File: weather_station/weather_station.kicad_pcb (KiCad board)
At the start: 2 copper layers, 72.5 x 42.5 mm, 76 parts, among them J1 USB_C_Receptacle_USB2.0_16P, Q1 PMOS, Q2 S8050, Q3 S8050, SW1 SW_Push, SW2 SW_Push, SW3 SW_Push, U2 TLV62569, U3 TP4056-42-ESOP8, U5 Ai-Thinker-Ra-02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

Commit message: Adjusting components
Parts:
- added H2: MountingHole, weather_station_lib:mounting_hole_2, F.Cu at (81.8, 92.0)
- added H3: MountingHole, weather_station_lib:mounting_hole_2, F.Cu at (143.8, 92.0)
- added H4: MountingHole, weather_station_lib:mounting_hole_2, F.Cu at (143.8, 127.0)
- H1: footprint weather_station_lib:mounting_hole_1.5 -> weather_station_lib:mounting_hole_2
- J1: footprint Connector_USB:USB_C_Receptacle_GCT_USB4105-xx-A_16P_TopMnt_Horizontal -> weather_station_lib:USB_C_Receptacle_GCT_USB4105-xx-A_16P_TopMnt_Horizontal_fix_clearance
- U1: footprint weather_station_lib:ESP32-WROOM-32 or ESP32S -> weather_station_lib:ESP32-WROOM-32 or ESP32S_no_paste
- U5: footprint RF_Module:Ai-Thinker-Ra-01-LoRa -> weather_station_lib:Ai-Thinker-Ra-01-LoRa_no_paste
- moved R15 181.1 mm to (87.6, 98.0)
- moved R13 179.8 mm to (87.6, 96.0), turned to 180 degrees
- moved C13 142.8 mm to (120.0, 95.0), turned to 180 degrees
- moved C14 141.9 mm to (119.8, 92.4), turned to 180 degrees
- moved TP1 140.2 mm to (86.4, 127.6)
- moved C17 137.7 mm to (110.6, 96.0), turned to 180 degrees
- moved C18 133.2 mm to (114.8, 96.8)
- moved R8 124.5 mm to (99.6, 94.8)
- moved U4 123.2 mm to (130.3, 96.5), turned to 90 degrees
- moved R18 123.2 mm to (90.8, 108.0)
- moved R11 122.9 mm to (124.3, 126.0)
- moved C8 122.9 mm to (122.3, 125.8)
- moved R2 122.8 mm to (103.4, 92.8), turned to 180 degrees
- moved Q3 122.5 mm to (95.8, 115.2), turned to 90 degrees
- moved R26 121.8 mm to (99.2, 112.2), turned to 0 degrees
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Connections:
- U6 pad 1: GND -> /SDA1
- U6 pad 2: +Vin -> /SCL1
- U6 pad 3: /SCL1 -> +Vin
- U6 pad 4: /SDA1 -> GND
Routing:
- net +Vin: track 0.00 -> 106.6 mm, vias 0 -> 3
- net /GPIO0: track 0.00 -> 65.9 mm, vias 0 -> 2
- net /TXD0: track 0.00 -> 56.0 mm, vias 0 -> 3
- net /EN: track 0.00 -> 55.4 mm, vias 0 -> 3
- net /VBAT_S: track 0.00 -> 53.6 mm, vias 0 -> 2
- net /RXD0: track 0.00 -> 52.9 mm, vias 0 -> 2
- net +Vbat: track 0.00 -> 43.9 mm, vias 0 -> 2
- net /SDA0: track 0.00 -> 43.0 mm, vias 0 -> 1
- net /SCL0: track 0.00 -> 40.7 mm, vias 0 -> 1
- net /SDA1: track 0.00 -> 37.7 mm, vias 0 -> 1
- net +Vch: track 0.00 -> 36.0 mm, vias 0 -> 3
- net VDDcp: track 0.00 -> 35.4 mm, vias 0 -> 3
- net /SCL1: track 0.00 -> 33.7 mm, vias 0 -> 1
- net /TFT_RST: track 0.00 -> 30.4 mm, vias 0 -> 1
- net /SPI_CLK: track 0.00 -> 28.6 mm
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- added copper zone on F.Cu, net +Vin
- added copper zone on B.Cu, net GND
- added copper zone on F.Cu, net GND
- added copper zone on F.Cu, net Net-(U2-SW)
- added copper zone on F.Cu, net Vusb
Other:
- board size 72.5 x 42.5 mm -> 67 x 40 mm
- board text added: "+"
- board text added: "-"
- board text added: "CHR"
- board text added: "EKM"
- board text added: "EN"
- board text added: "RX"
- board text added: "Rev0.1"
- board text added: "TX"

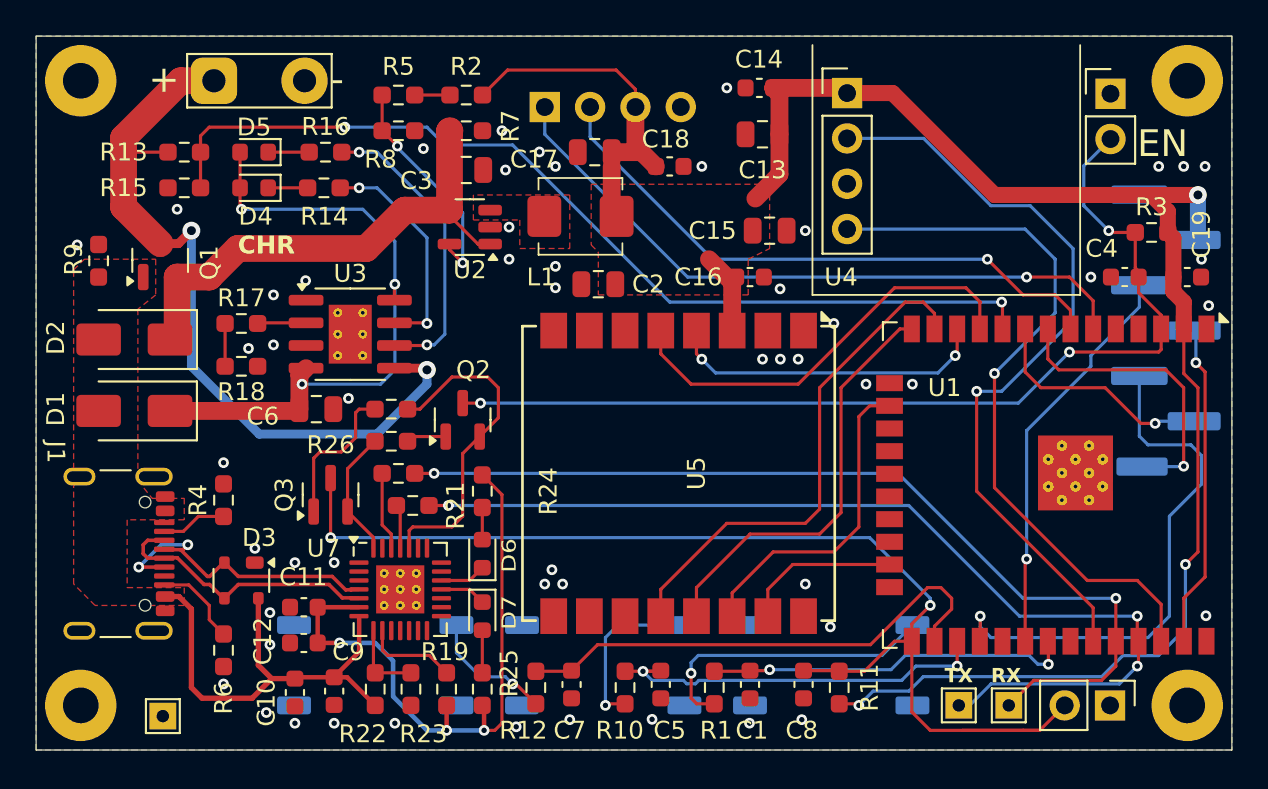
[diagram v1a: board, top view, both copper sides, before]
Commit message: Adjust min via hole size to 0.3mm
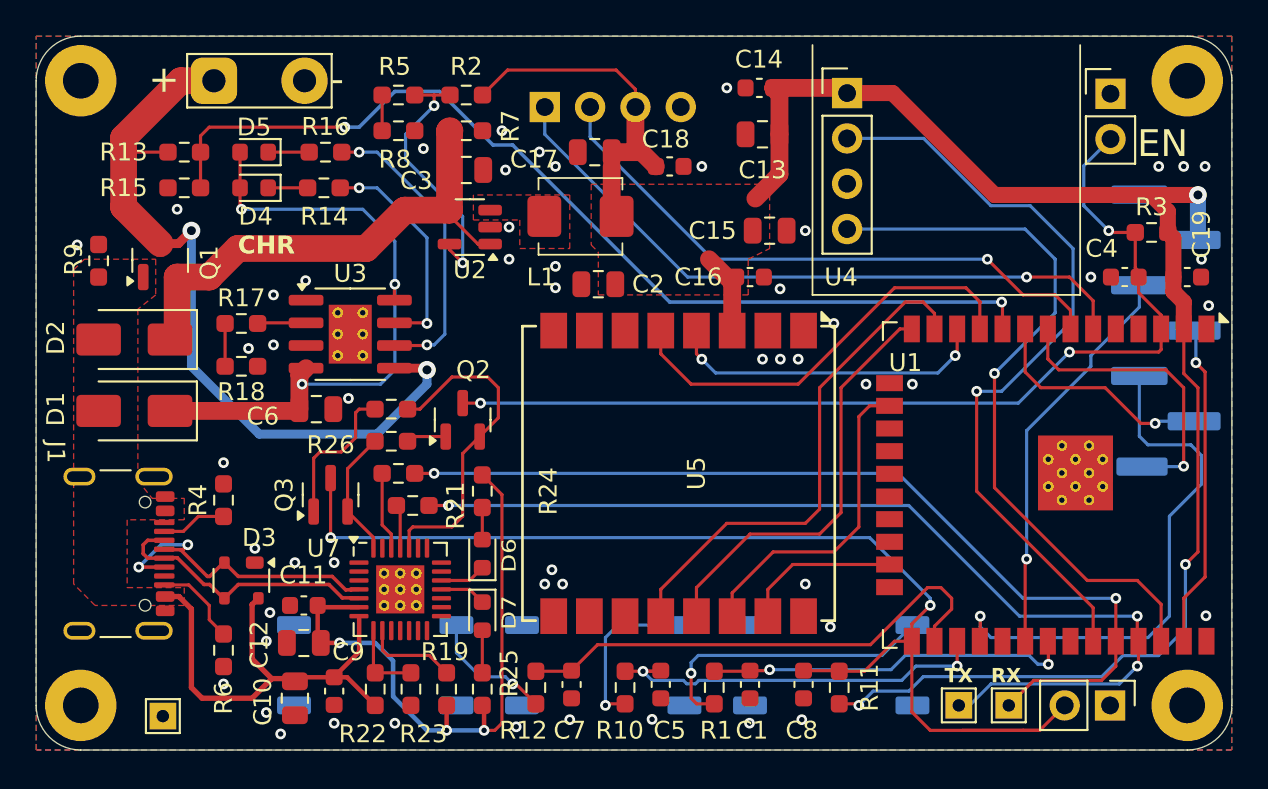
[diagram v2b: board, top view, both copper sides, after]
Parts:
- C10, C12: footprint Capacitor_SMD:C_0603_1608Metric -> Capacitor_SMD:C_0805_2012Metric
- Q2, Q3: value S8050 -> MMBT3904
- R2, R7: value 390k -> 470k
- R22: value 22k1 -> 22k
- R23: value 47k5 -> 47k
- R5: value 22k1 -> 12k
- U3: footprint Package_SO:SOIC-8-1EP_3.9x4.9mm_P1.27mm_EP2.41x3.3mm_ThermalVias -> weather_station_lib:SOIC-8-1EP_3.9x4.9mm_P1.27mm_EP2.41x3.3mm_ThermalVias_via_0.3mm
- U7: footprint Package_DFN_QFN:QFN-28-1EP_5x5mm_P0.5mm_EP2.7x2.7mm_ThermalVias -> weather_station_lib:QFN-28-1EP_5x5mm_P0.5mm_EP2.7x2.7mm_ThermalVias_via_0.3mm
- moved C10 0.32 mm to (93.8, 126.6)
- moved C11 0.10 mm to (94.3, 121.4)
- turned R5 to 0 degrees
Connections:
- R2 pad 2: Net-(R2-Pad2) -> Net-(U2-FB)
- R5 pad 1: Net-(R2-Pad2) -> Net-(R5-Pad1)
- R8 pad 2: Net-(U2-FB) -> Net-(R5-Pad1)
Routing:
- net Net-(U2-FB): track 12.6 -> 14.7 mm
- net Net-(R5-Pad1): track 0.00 -> 2.00 mm
- net Net-(R2-Pad2): track 1.97 -> 0.00 mm
- net /VBAT_S: track 53.6 -> 55.2 mm
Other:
- outline, holes or cut-outs redrawn
